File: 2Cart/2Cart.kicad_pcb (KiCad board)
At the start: 2 copper layers, 90 x 56.8 mm, 11 parts, among them J1 CommanderX16Expansion Alt, U1 SST39SF040, U2 74HCT00, U3 74HCT138, U4 AS6C4008-55PCN

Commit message: Verification, changes
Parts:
- JP1: value Jumper_2_Bridged -> WRITE EN
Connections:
- J1 pad 10: Net-(J1-ROMB0) -> ROMB0
- J1 pad 12: Net-(J1-ROMB1) -> ROMB1
- J1 pad 16: Net-(J1-ROMB2) -> ROMB2
- J1 pad 20: Net-(J1-ROMB3) -> ROMB3
- J1 pad 22: Net-(J1-ROMB4) -> ROMB4
- J1 pad 30: Net-(J1-D0) -> D0
- J1 pad 31: Net-(J1-A0) -> A0
- J1 pad 32: Net-(J1-D1) -> D1
- J1 pad 33: Net-(J1-A1) -> A1
- J1 pad 34: Net-(J1-D2) -> D2
- J1 pad 35: Net-(J1-A2) -> A2
- J1 pad 36: Net-(J1-D3) -> D3
- J1 pad 37: Net-(J1-A3) -> A3
- J1 pad 38: Net-(J1-D4) -> D4
- J1 pad 39: Net-(J1-A4) -> A4
- J1 pad 40: Net-(J1-D5) -> D5
- J1 pad 41: Net-(J1-A5) -> A5
- J1 pad 42: Net-(J1-D6) -> D6
- J1 pad 43: Net-(J1-A6) -> A6
- J1 pad 44: Net-(J1-D7) -> D7
- J1 pad 45: Net-(J1-A7) -> A7
- J1 pad 47: Net-(J1-A8) -> A8
- J1 pad 49: Net-(J1-A9) -> A9
- J1 pad 50: Net-(J1-A13) -> A13
- J1 pad 51: Net-(J1-A10) -> A10
- J1 pad 52: Net-(J1-A12) -> A12
- J1 pad 53: Net-(J1-A11) -> A11
- U1 pad 1: Net-(J1-ROMB4) -> ROMB4
- U1 pad 10: Net-(J1-A2) -> A2
- U1 pad 11: Net-(J1-A1) -> A1
- U1 pad 12: Net-(J1-A0) -> A0
- U1 pad 13: Net-(J1-D0) -> D0
- U1 pad 14: Net-(J1-D1) -> D1
- U1 pad 15: Net-(J1-D2) -> D2
- U1 pad 17: Net-(J1-D3) -> D3
- U1 pad 18: Net-(J1-D4) -> D4
- U1 pad 19: Net-(J1-D5) -> D5
- U1 pad 2: Net-(J1-ROMB2) -> ROMB2
- U1 pad 20: Net-(J1-D6) -> D6
- U1 pad 21: Net-(J1-D7) -> D7
- U1 pad 23: Net-(J1-A10) -> A10
- U1 pad 25: Net-(J1-A11) -> A11
- U1 pad 26: Net-(J1-A9) -> A9
- U1 pad 27: Net-(J1-A8) -> A8
- U1 pad 28: Net-(J1-A13) -> A13
- U1 pad 29: Net-(J1-ROMB0) -> ROMB0
- U1 pad 3: Net-(J1-ROMB1) -> ROMB1
- U1 pad 30: Net-(J1-ROMB3) -> ROMB3
- U1 pad 4: Net-(J1-A12) -> A12
- U1 pad 5: Net-(J1-A7) -> A7
- U1 pad 6: Net-(J1-A6) -> A6
- U1 pad 7: Net-(J1-A5) -> A5
- U1 pad 8: Net-(J1-A4) -> A4
- U1 pad 9: Net-(J1-A3) -> A3
- U3 pad 14: unconnected-(U3-~{Y1}-Pad14) -> !RAMBEN
- U4 pad 1: unconnected-(U4-A18-Pad1) -> ROMB4
- U4 pad 10: unconnected-(U4-A2-Pad10) -> A2
- U4 pad 11: unconnected-(U4-A1-Pad11) -> A1
- U4 pad 12: unconnected-(U4-A0-Pad12) -> A0
- U4 pad 13: unconnected-(U4-DQ0-Pad13) -> D0
- U4 pad 14: unconnected-(U4-DQ1-Pad14) -> D1
- U4 pad 15: unconnected-(U4-DQ2-Pad15) -> D2
- U4 pad 16: unconnected-(U4-VSS-Pad16) -> GND
- U4 pad 17: unconnected-(U4-DQ3-Pad17) -> D3
- U4 pad 18: unconnected-(U4-DQ4-Pad18) -> D4
- U4 pad 19: unconnected-(U4-DQ5-Pad19) -> D5
- U4 pad 2: unconnected-(U4-A16-Pad2) -> ROMB2
- U4 pad 20: unconnected-(U4-DQ6-Pad20) -> D6
- U4 pad 21: unconnected-(U4-DQ7-Pad21) -> D7
- U4 pad 22: unconnected-(U4-CE#-Pad22) -> !RAMBEN
- U4 pad 23: unconnected-(U4-A10-Pad23) -> A10
- U4 pad 24: unconnected-(U4-OE#-Pad24) -> !MEMOE
- U4 pad 25: unconnected-(U4-A11-Pad25) -> A11
- U4 pad 26: unconnected-(U4-A9-Pad26) -> A9
- U4 pad 27: unconnected-(U4-A8-Pad27) -> A8
- U4 pad 28: unconnected-(U4-A13-Pad28) -> A13
- U4 pad 29: unconnected-(U4-WE#-Pad29) -> !MEMWE
- U4 pad 3: unconnected-(U4-A14-Pad3) -> ROMB0
- U4 pad 30: unconnected-(U4-A17-Pad30) -> ROMB3
- U4 pad 31: unconnected-(U4-A15-Pad31) -> ROMB1
- U4 pad 4: unconnected-(U4-A12-Pad4) -> A12
- U4 pad 5: unconnected-(U4-A7-Pad5) -> A7
- U4 pad 6: unconnected-(U4-A6-Pad6) -> A6
- U4 pad 7: unconnected-(U4-A5-Pad7) -> A5
- U4 pad 8: unconnected-(U4-A4-Pad8) -> A4
- U4 pad 9: unconnected-(U4-A3-Pad9) -> A3

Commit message: Flip the board
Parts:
- C1, C2, C3: value C -> 100nF
- C4: value C -> 100nF; moved to B.Cu
- U1: value SST39SF040 -> SST39SF040 (ROM)
- U4: value AS6C4008-55PCN -> AS6C4008 (RAM)
- moved C3 7.76 mm to (71.8, 84.0)
- moved C1 6.25 mm to (99.0, 102.0)
- moved C4 5.77 mm to (81.5, 94.5)
- moved R1 5.29 mm to (120.0, 101.8)
- moved U2 2.43 mm to (76.0, 97.6)
- moved C2 2.30 mm to (68.0, 107.5)
- moved JP1 2.25 mm to (108.2, 101.8)
- moved U3 1.34 mm to (78.7, 120.3)
- moved U4 1.00 mm to (130.6, 81.9)
- moved U1 0.25 mm to (130.6, 121.4)

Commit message: Routing yikes
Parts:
- moved C4 54.1 mm to (135.0, 86.5), turned to -90 degrees
- moved R1 39.2 mm to (81.0, 106.0), turned to -90 degrees
- moved C1 37.5 mm to (134.0, 115.5), turned to 90 degrees
- moved JP1 27.3 mm to (81.0, 100.0), turned to -90 degrees
- moved C2 12.5 mm to (55.5, 107.5)
- moved U3 4.75 mm to (73.9, 120.3)
- moved U2 4.33 mm to (71.6, 97.6)
- moved U1 1.51 mm to (129.1, 121.2)
- moved U4 0.07 mm to (130.5, 81.9)
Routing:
- net GND: track 0.00 -> 221.2 mm
- net +5V: track 0.00 -> 136.3 mm
- net ROMB0: track 0.00 -> 118.4 mm, vias 0 -> 1
- net ROMB4: track 0.00 -> 95.0 mm, vias 0 -> 1
- net ROMB3: track 0.00 -> 77.8 mm, vias 0 -> 1
- net Net-(J1-A14): track 0.00 -> 67.2 mm, vias 0 -> 1
- net Net-(J1-A15): track 0.00 -> 66.7 mm, vias 0 -> 1
- net !MEMOE: track 0.00 -> 66.2 mm
- net D0: track 0.00 -> 62.0 mm, vias 0 -> 1
- net A7: track 0.00 -> 56.9 mm
- net A6: track 0.00 -> 56.9 mm
- net ROMB2: track 0.00 -> 56.0 mm
- net A3: track 0.00 -> 53.6 mm
- net A0: track 0.00 -> 53.5 mm
- net A1: track 0.00 -> 53.4 mm
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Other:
- copper layers 2 -> 4

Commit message: Routing madness
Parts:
- C1, C2, C3, C4: footprint Capacitor_THT:C_Disc_D5.0mm_W2.5mm_P5.00mm -> Capacitor_THT:C_Axial_L3.8mm_D2.6mm_P7.50mm_Horizontal
- U4: moved to B.Cu
- moved U4 17.1 mm to (130.2, 99.0), turned to 90 degrees
- moved C3 2.00 mm to (71.8, 86.0)
- moved C2 1.50 mm to (55.5, 109.0)
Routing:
- net !RAMBEN: track 0.00 -> 65.5 mm
- net GND: track 221.2 -> 164.4 mm
- net Net-(JP1-B): track 3.46 -> 50.4 mm
- net ROMB4: track 95.0 -> 55.6 mm
- net ROMB2: track 56.0 -> 91.7 mm, vias 0 -> 1
- net !ROMBEN: track 0.00 -> 35.1 mm
- net ROMB0: track 118.4 -> 84.3 mm
- net ROMB1: track 43.9 -> 62.5 mm, vias 2 -> 1
- net A3: track 53.6 -> 35.3 mm
- net A0: track 53.5 -> 35.3 mm
- net A1: track 53.4 -> 35.3 mm
- net A6: track 56.9 -> 38.7 mm
- net A12: track 51.3 -> 33.2 mm
- net A7: track 56.9 -> 38.8 mm
- net A5: track 53.3 -> 35.3 mm
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
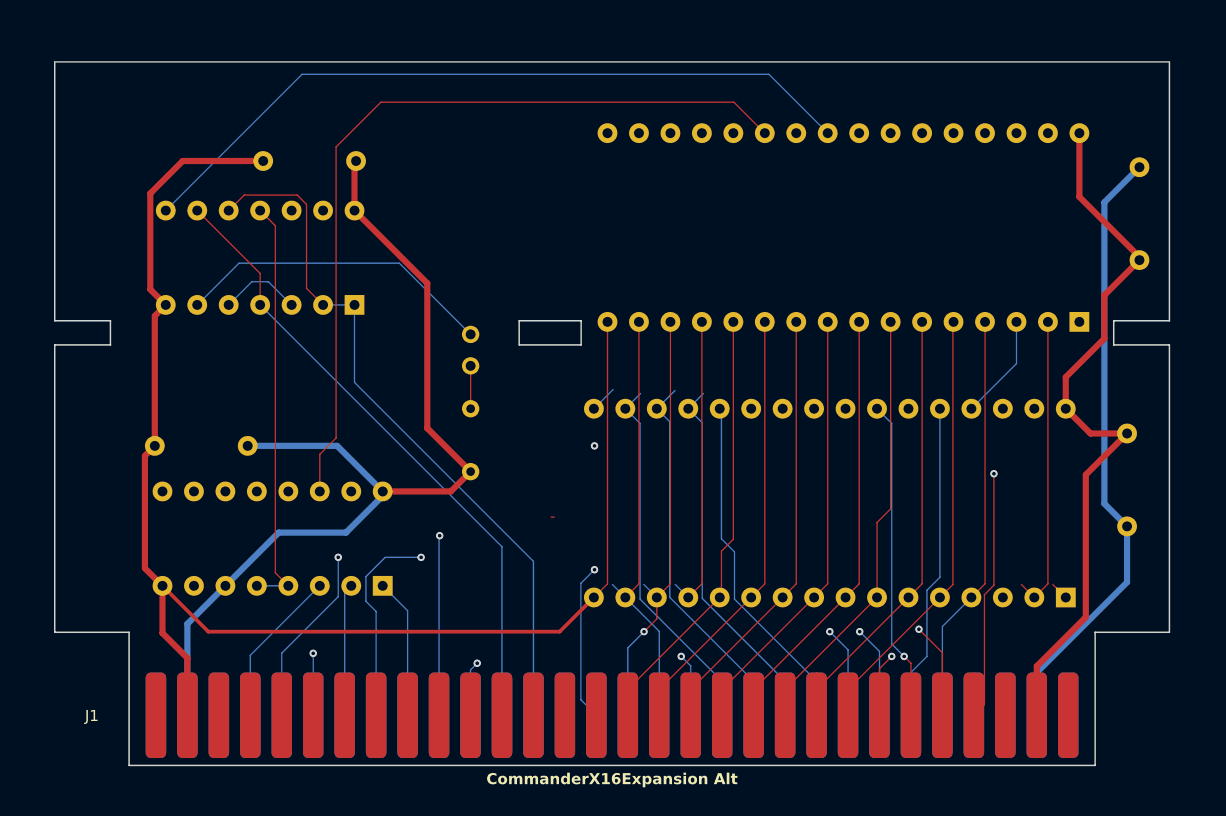
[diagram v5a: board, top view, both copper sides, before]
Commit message: Two layer routing with copper pours
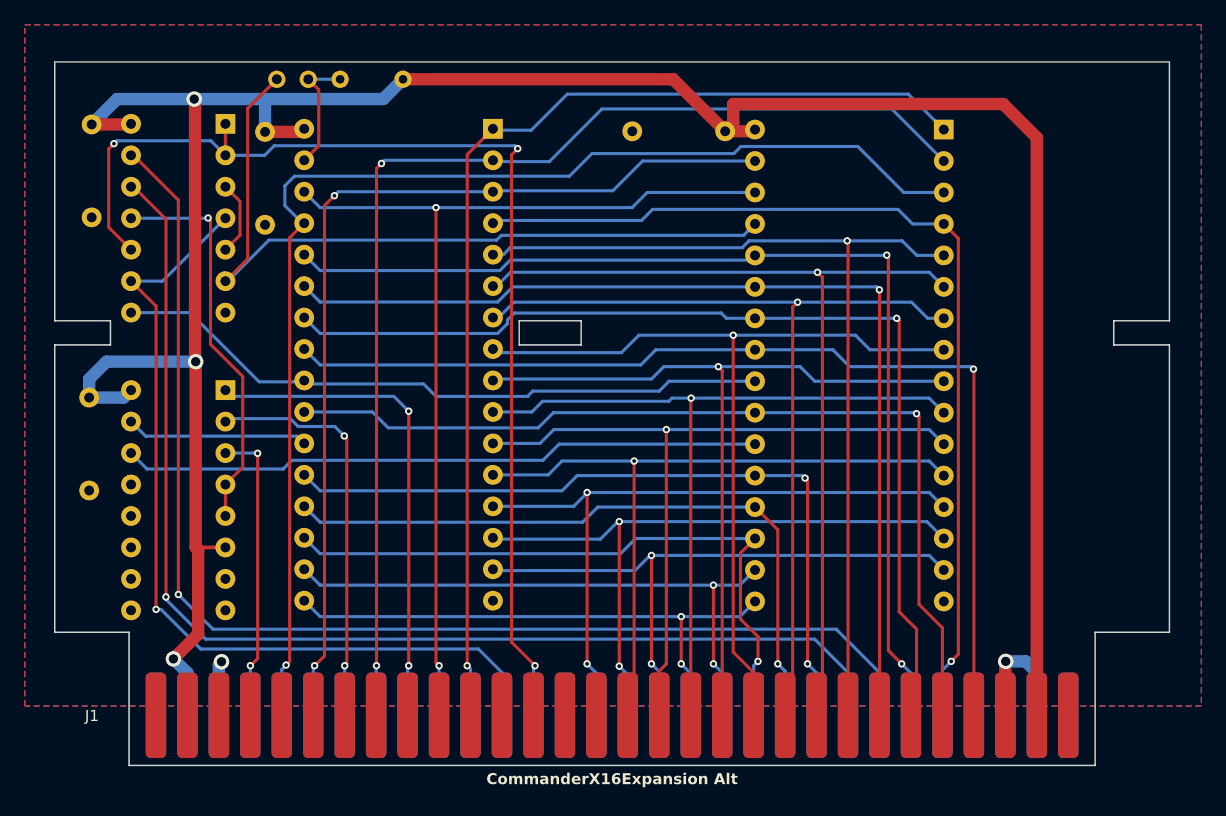
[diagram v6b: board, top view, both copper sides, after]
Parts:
- moved C1 73.7 mm to (64.4, 91.2)
- moved U1 59.8 mm to (82.8, 83.4), turned to 180 degrees
- moved C4 41.1 mm to (94.0, 83.6), turned to 0 degrees
- moved R1 28.6 mm to (70.5, 79.4), turned to 0 degrees
- moved JP1 25.9 mm to (65.3, 79.4), turned to 0 degrees
- moved C3 21.6 mm to (50.4, 83.0), turned to -90 degrees
- moved U3 20.3 mm to (61.2, 104.5), turned to 180 degrees
- moved U4 19.0 mm to (119.2, 83.5), turned to 180 degrees
- moved U2 18.0 mm to (61.2, 83.0), turned to 180 degrees
- moved C2 6.41 mm to (50.2, 112.6), turned to 90 degrees
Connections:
- net Net-(J1-A14) renamed /A14
- net Net-(J1-A15) renamed /A15
- net Net-(J1-PHI2) renamed /PHI2
- net Net-(J1-ROMB5) renamed /ROMB5
- net Net-(J1-ROMB6) renamed /ROMB6
- net Net-(J1-ROMB7) renamed /ROMB7
- net Net-(J1-RWB) renamed /RWB
- J1 pad 1: Net-(J1--12V-Pad1) -> unconnected-(J1--12V-Pad1)
- J1 pad 2: Net-(J1-+12V-Pad2) -> unconnected-(J1-+12V-Pad2)
- J1 pad 59: Net-(J1-+12V-Pad2) -> unconnected-(J1-+12V-Pad2)_1
- J1 pad 60: Net-(J1--12V-Pad1) -> unconnected-(J1--12V-Pad1)_1
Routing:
- net GND: track 164.4 -> 15.1 mm, vias 0 -> 2
- net +5V: track 135.3 -> 208.5 mm, vias 0 -> 3
- net A13: track 25.7 -> 85.5 mm, vias 0 -> 2
- net A9: track 25.9 -> 81.7 mm
- net A8: track 27.5 -> 81.9 mm
- net A11: track 37.8 -> 83.7 mm
- net A10: track 30.1 -> 75.7 mm
- net A12: track 33.2 -> 77.7 mm, vias 0 -> 1
- net Net-(JP1-B): track 50.4 -> 9.95 mm
- net A7: track 38.8 -> 75.7 mm, vias 0 -> 1
- net !MEMWE: track 25.9 -> 62.7 mm
- net /RWB: track 57.4 -> 92.4 mm, vias 0 -> 3
- net A5: track 35.3 -> 69.9 mm, vias 0 -> 1
- net A6: track 38.7 -> 72.8 mm, vias 0 -> 1
- net A4: track 35.3 -> 68.5 mm, vias 0 -> 1
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- added copper zone on B.Cu, net GND
- added copper zone on F.Cu, net GND
- added copper zone on In1.Cu, net GND
- added copper zone on In2.Cu, net GND

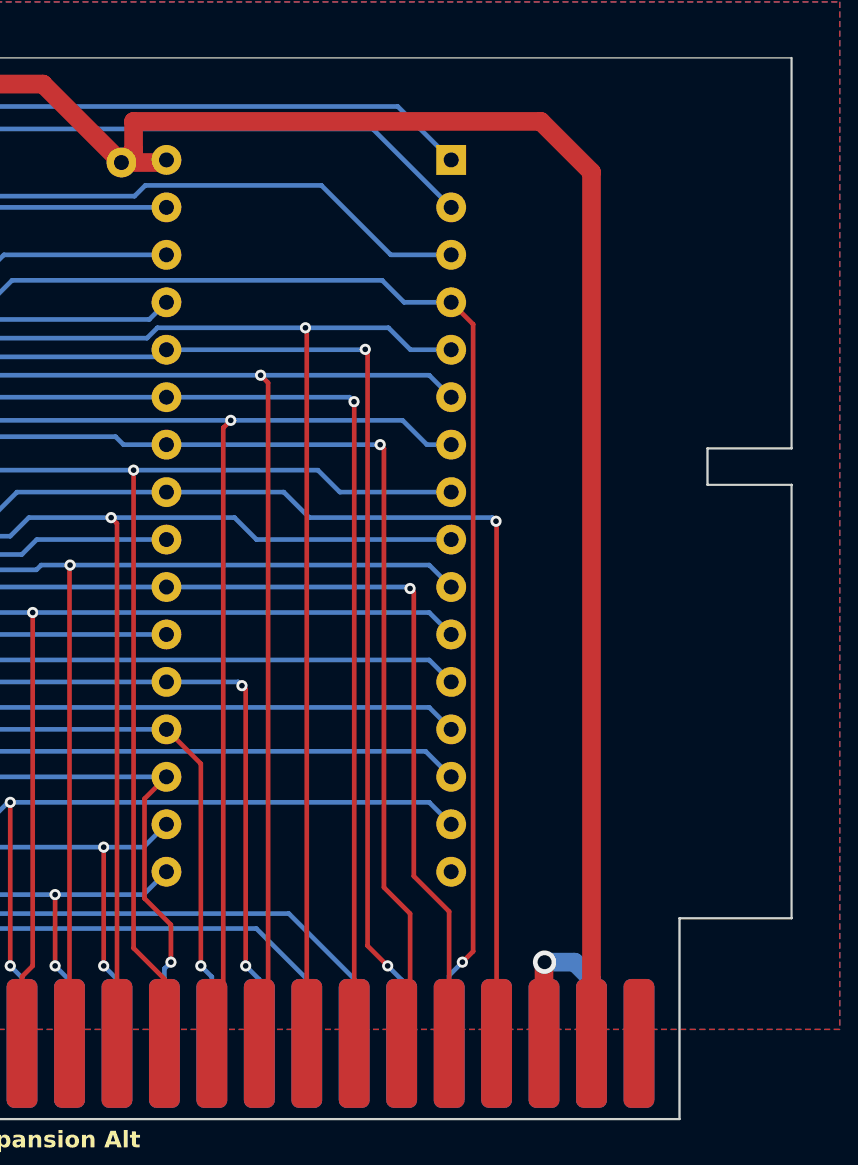
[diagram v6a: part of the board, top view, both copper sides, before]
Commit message: Added I2C NVRAM
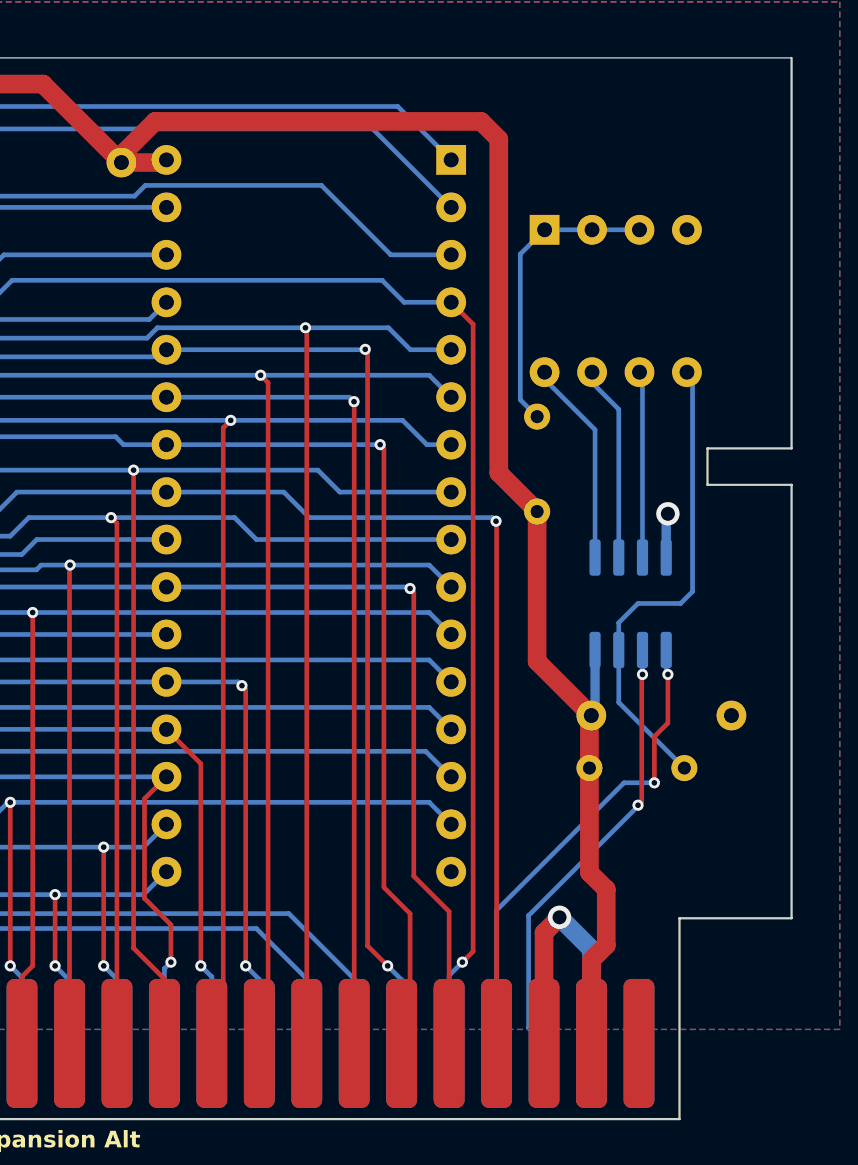
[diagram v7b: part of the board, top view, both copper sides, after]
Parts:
- added C5: 100nF, Capacitor_THT:C_Axial_L3.8mm_D2.6mm_P7.50mm_Horizontal, B.Cu at (134.2, 113.2)
- added R2: 100K, Resistor_THT:R_Axial_DIN0204_L3.6mm_D1.6mm_P5.08mm_Horizontal, B.Cu at (131.7, 116.0)
- added R3: 100K, Resistor_THT:R_Axial_DIN0204_L3.6mm_D1.6mm_P5.08mm_Horizontal, B.Cu at (123.8, 102.3)
- added SW1: SW_DIP_x04, Button_Switch_THT:SW_DIP_SPSTx04_Slide_9.78x12.34mm_W7.62mm_P2.54mm, B.Cu at (124.2, 87.2)
- added U5: FM24C64B, Package_SO:SOIC-8_3.9x4.9mm_P1.27mm, B.Cu at (128.8, 107.2)
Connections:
- J1 pad 54: unconnected-(J1-SDA-Pad54) -> /SDA
- J1 pad 56: unconnected-(J1-SCL-Pad56) -> /SCL
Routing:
- net /SDA: track 0.00 -> 25.8 mm, vias 0 -> 2
- net /WP: track 0.00 -> 25.7 mm
- net /SCL: track 0.00 -> 23.6 mm, vias 0 -> 2
- net Net-(R3-Pad2): track 0.00 -> 16.0 mm
- net /FA0: track 0.00 -> 11.0 mm
- net /FA1: track 0.00 -> 10.5 mm
- net /FA2: track 0.00 -> 9.99 mm
- net GND: track 15.1 -> 21.3 mm, vias 2 -> 3
- net +5V: track 208.5 -> 210.3 mm
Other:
- board text added: "A0"
- board text added: "A1"
- board text added: "A2"
- board text added: "NVRAM Addr"
- board text added: "NVRAM Wr. Prot."
